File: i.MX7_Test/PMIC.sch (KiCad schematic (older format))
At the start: 0 parts

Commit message: finished DDR3L RAM for 1GB with 2 banks
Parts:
- added U?: PF3000, symbol PF3000
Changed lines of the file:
@@
 LIBS:IMX7D
 LIBS:voltages
+LIBS:pf3000
 LIBS:i.MX7_Test-cache
 EELAYER 25 0
@@
 Comment4 ""
 $EndDescr
+$Comp
+L PF3000 U?
+U 1 1 591F927C
+P 6800 3250
+F 0 "U?" H 6800 3250 60  0000 C CNN
+F 1 "PF3000" H 6800 3250 60  0000 C CNN
+F 2 "" H 6800 3250 60  0001 C CNN
+F 3 "" H 6800 3250 60  0001 C CNN
+	1    6800 3250
+	1    0    0    -1
+$EndComp
 $EndSCHEMATC

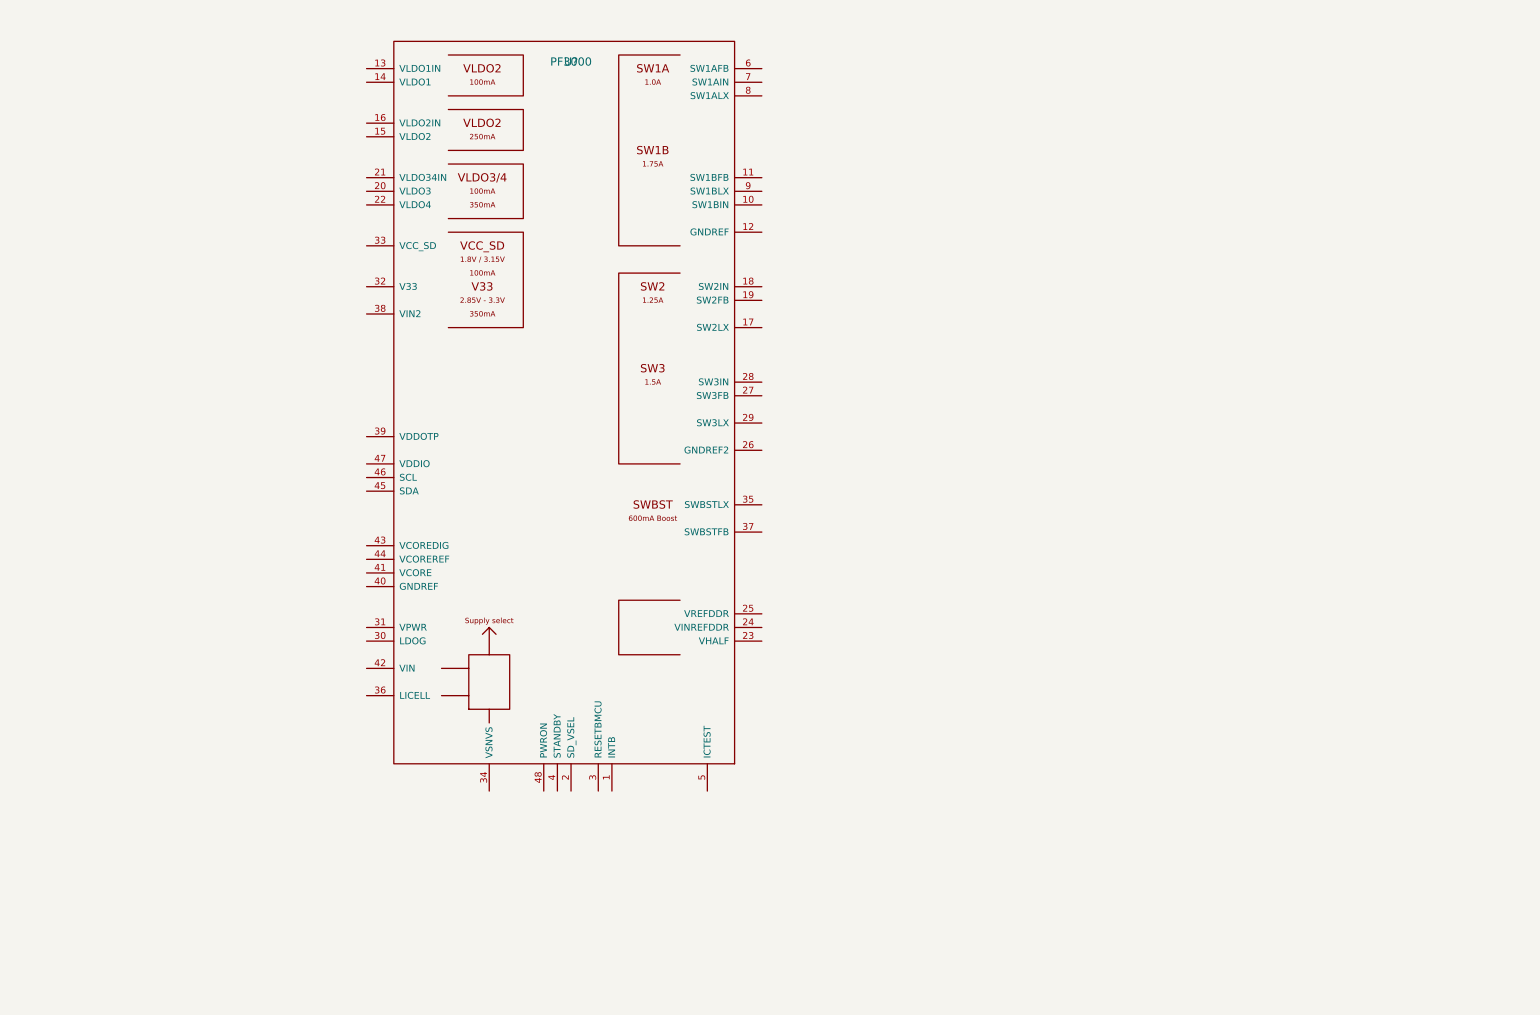
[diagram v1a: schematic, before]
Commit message: Added some schematics for PMIC Added some Documentation for i.mx7
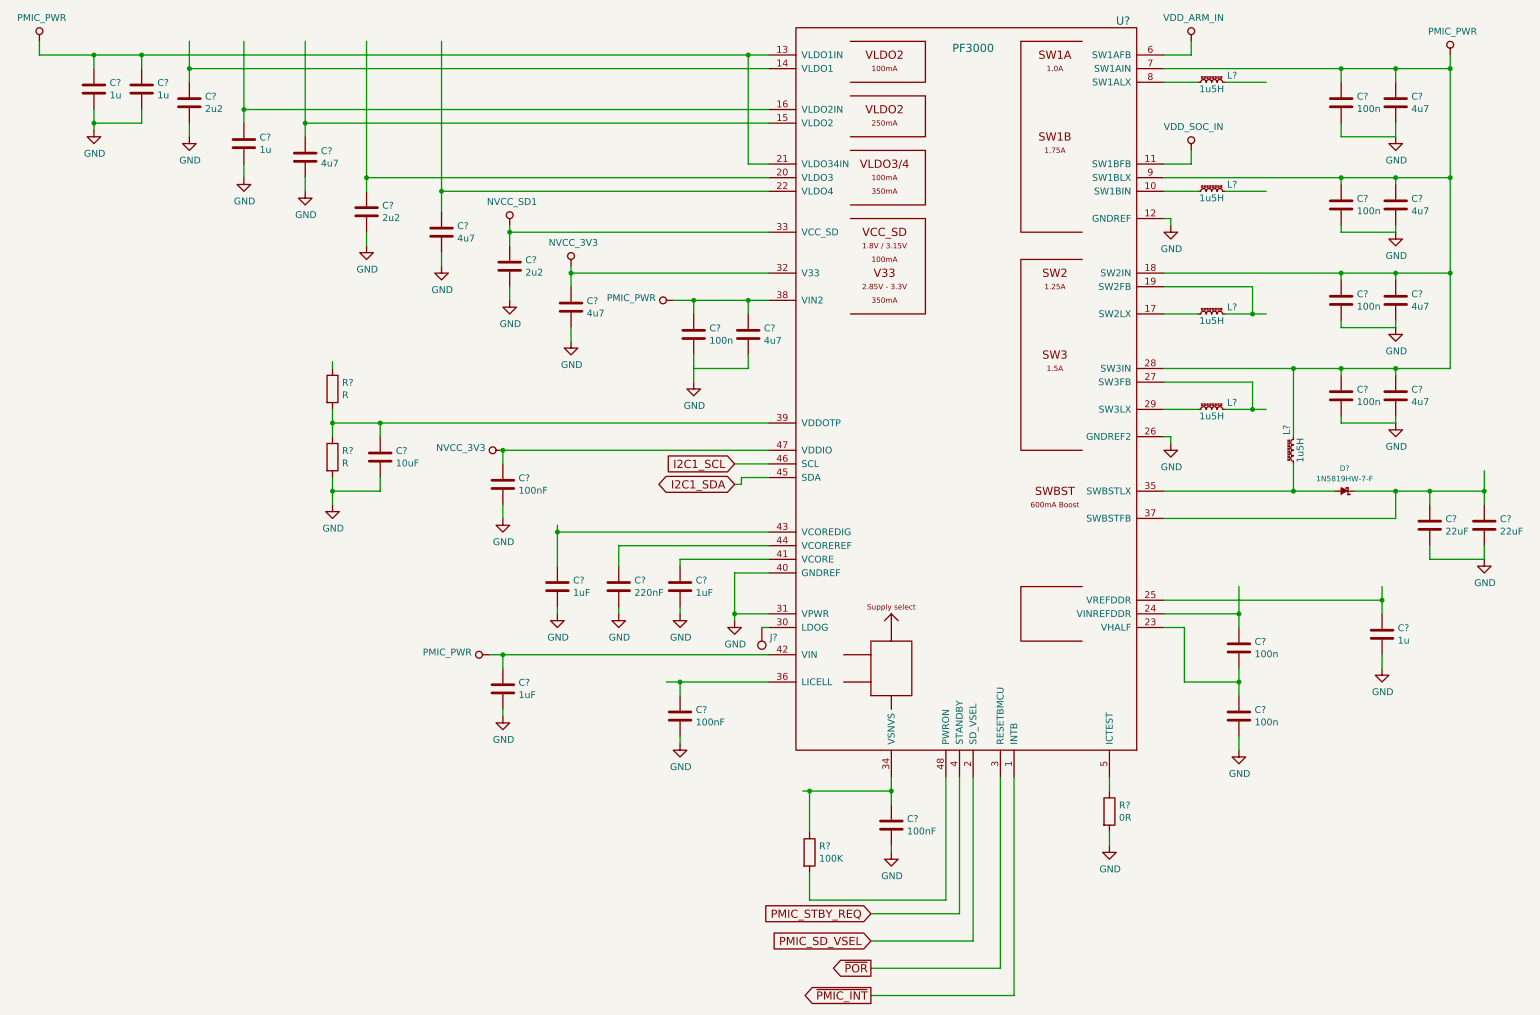
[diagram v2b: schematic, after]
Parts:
- added C? (x4): 1u, symbol C
- added C? (x7): 100n, symbol C
- added C? (x3): 2u2, symbol C
- added C? (x8): 4u7, symbol C
- added C? (x2): 22uF, symbol C
- added C?: 10uF, symbol C
- added C? (x3): 100nF, symbol C
- added C? (x3): 1uF, symbol C
- added C?: 220nF, symbol C
- added D?: 1N5819HW-7-F, symbol SCHOTTKY
- added J?: TEST_1P, symbol TEST_1P
- added L? (x5): 1u5H, symbol L_Core_Ferrite_Small
- added R? (x2): R, symbol R
- added R?: 0R, symbol R
- added R?: 100K, symbol R
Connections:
- net labels added: GND, I2C1_SCL, I2C1_SDA, NVCC_3V3, NVCC_SD1, PMIC_PWR, PMIC_SD_VSEL, PMIC_STBY_REQ, VDD_ARM_IN, VDD_SOC_IN, ~PMIC_INT, ~POR
- wire segments 0 -> 195
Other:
- moved on the sheet: U?
